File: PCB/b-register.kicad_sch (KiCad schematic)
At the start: 20 parts, among them U7 74LS245, U8 74LS173, U9 74LS173

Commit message: added more models to work with on my pcb
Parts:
- D022, D023, D024, D025, D026, D027, D028, D029: footprint LED_THT:LED_D1.8mm_W1.8mm_H2.4mm_Horizontal_O1.27mm_Z1.6mm -> LED_THT:LED_D3.0mm
- U7: footprint (none) -> Custom:DIP254P762X508-20
- U8, U9: footprint (none) -> Custom:SN74LS173AN
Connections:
- net GND: now also U7.10 (GND), U8.8 (GND), U9.8 (GND)
- net VCC: now also U7.20 (VCC), U8.16 (VCC), U9.16 (VCC)

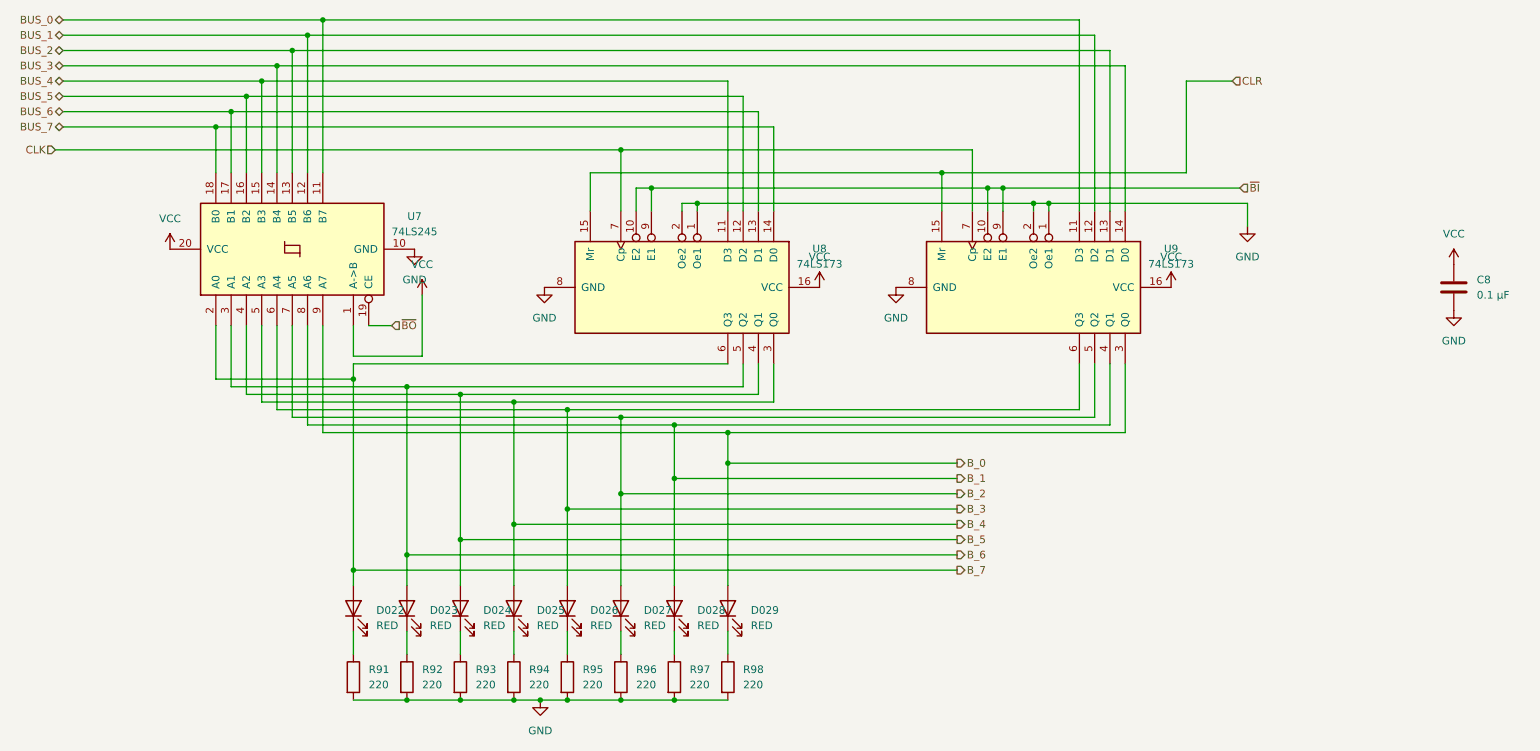
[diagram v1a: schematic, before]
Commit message: Fixed a bunch of ERC errors so know there is only one remaining.
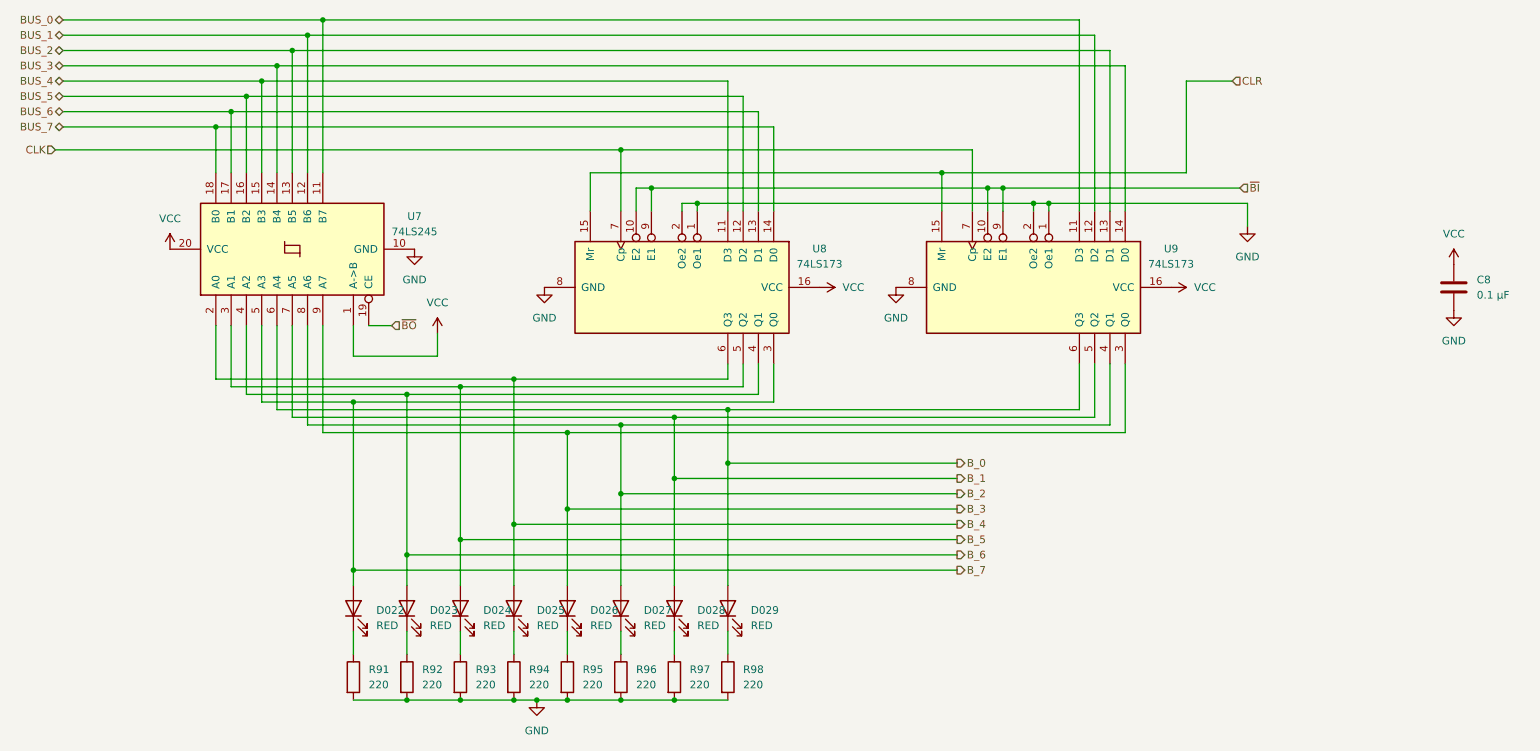
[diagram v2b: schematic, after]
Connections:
- net B_0: now also U7.6 (A4), U9.6 (Q3); no longer U7.9 (A7), U9.3 (Q0)
- net B_1: now also U7.7 (A5), U9.5 (Q2); no longer U7.8 (A6), U9.4 (Q1)
- net B_2: now also U7.8 (A6), U9.4 (Q1); no longer U7.7 (A5), U9.5 (Q2)
- net B_3: now also U7.9 (A7), U9.3 (Q0); no longer U7.6 (A4), U9.6 (Q3)
- net B_4: now also U7.2 (A0), U8.6 (Q3); no longer U7.5 (A3), U8.3 (Q0)
- net B_5: now also U7.3 (A1), U8.5 (Q2); no longer U7.4 (A2), U8.4 (Q1)
- net B_6: now also U7.4 (A2), U8.4 (Q1); no longer U7.3 (A1), U8.5 (Q2)
- net B_7: now also U7.5 (A3), U8.3 (Q0); no longer U7.2 (A0), U8.6 (Q3)

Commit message: Add decupling caps and reroute pcb. Updated BOM to match new number of caps
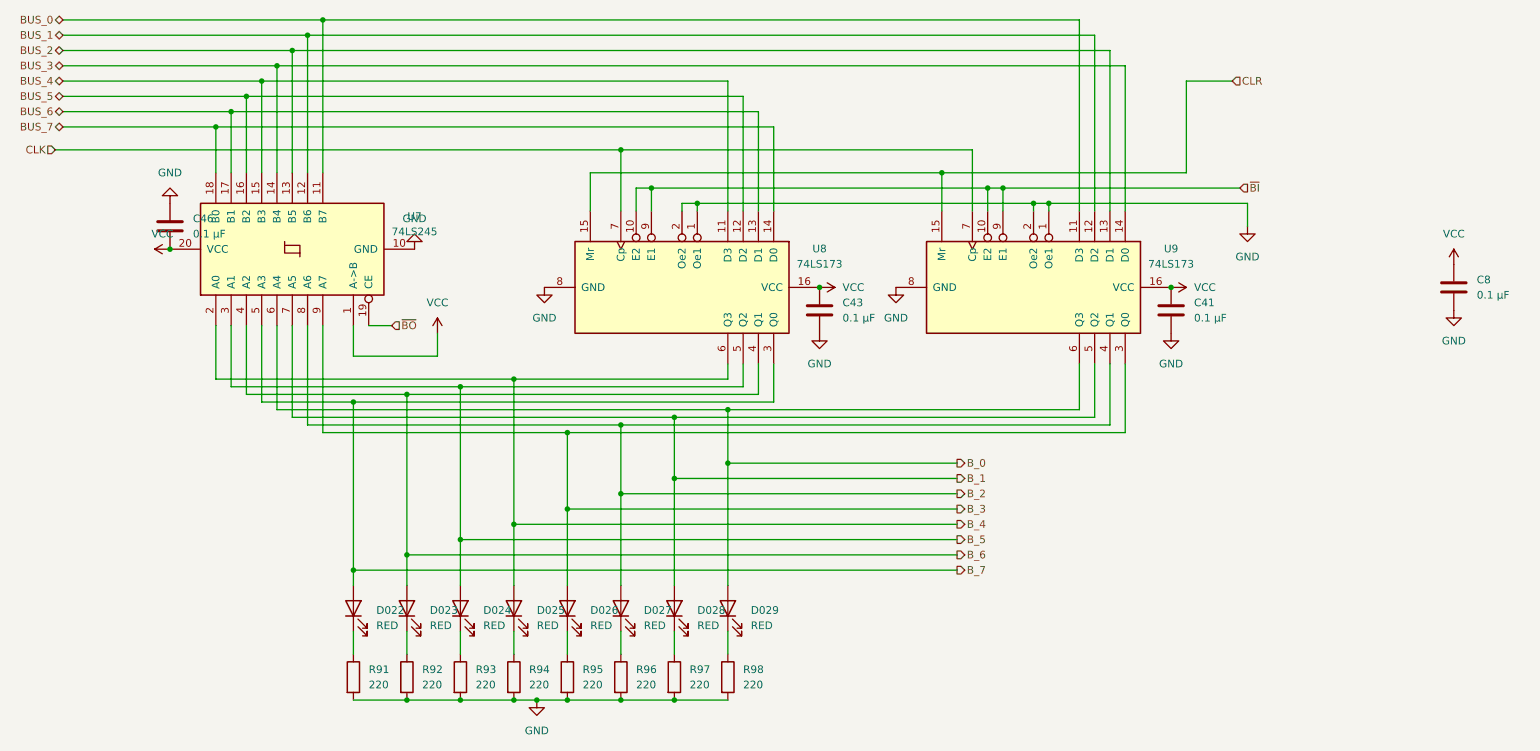
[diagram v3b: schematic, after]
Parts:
- added C41, C43, C46: 0.1 µF, Capacitor_THT:C_Radial_D5.0mm_H5.0mm_P2.00mm, symbol Device:C
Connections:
- net GND: now also C41.2, C43.2, C46.1
- net VCC: now also C41.1, C43.1, C46.2

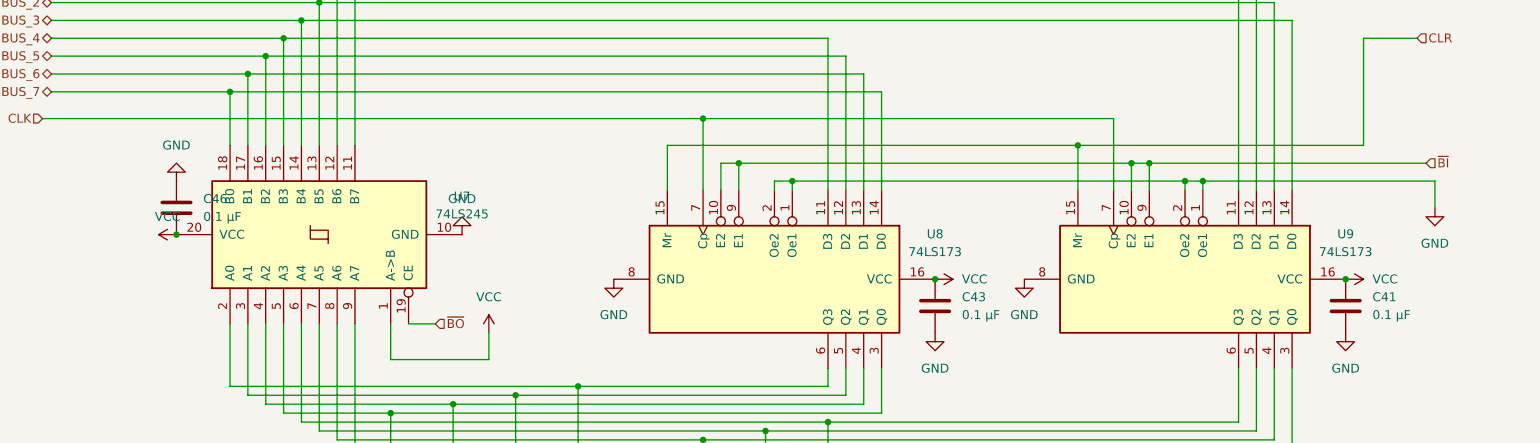
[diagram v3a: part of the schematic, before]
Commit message: Redoing PCB layout and fixed some signal flow convention errors
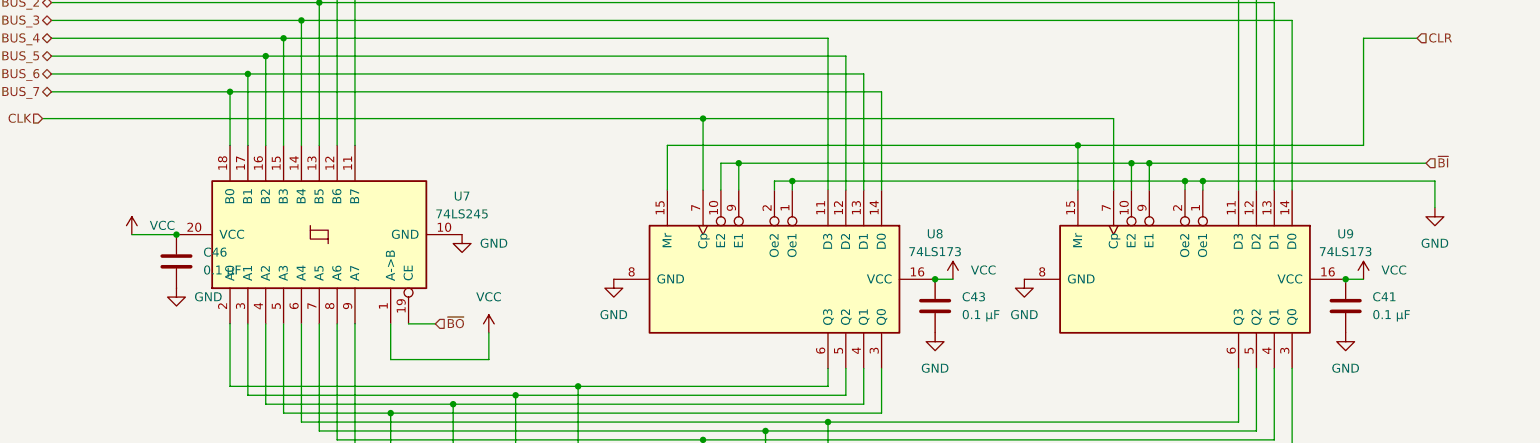
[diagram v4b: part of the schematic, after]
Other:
- moved on the sheet: C46
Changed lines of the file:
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@@
 	)
 	(junction
-		(at 46.99 58.42)
-		(diameter 0)
-		(color 0 0 0 0)
-	)
-	(junction
 		(at 185.42 48.26)
 		(diameter 0)
@@
 	)
 	(junction
+		(at 46.99 58.42)
+		(diameter 0)
+		(color 0 0 0 0)
+	)
+	(junction
 		(at 95.25 81.28)
 		(diameter 0)
@@
 	(wire
 		(pts
+			(xy 157.48 64.77) (xy 154.94 64.77)
+		)
+		(stroke
+			(width 0)
+			(type default)
+		)
+	)
+	(wire
+		(pts
 			(xy 69.85 87.63) (xy 121.92 87.63)
 		)
@@
 	(wire
 		(pts
+			(xy 40.64 58.42) (xy 46.99 58.42)
+		)
+		(stroke
+			(width 0)
+			(type default)
+		)
+	)
+	(wire
+		(pts
 			(xy 144.78 35.56) (xy 144.78 52.07)
 		)
@@
 	(wire
 		(pts
+			(xy 215.9 64.77) (xy 213.36 64.77)
+		)
+		(stroke
+			(width 0)
+			(type default)
+		)
+	)
+	(wire
+		(pts
 			(xy 29.21 22.86) (xy 69.85 22.86)
 		)
@@
 	(symbol
 		(lib_id "power:VCC")
-		(at 213.36 64.77 270)
+		(at 215.9 64.77 0)
 		(unit 1)
 		(exclude_from_sim no)
@@
 		(fields_autoplaced yes)
 		(property "Reference" "#PWR0134"
-			(at 209.55 64.77 0)
+			(at 215.9 68.58 0)
 			(effects
 				(font
@@
 		)
 		(property "Value" "VCC"
-			(at 217.17 64.7699 90)
+			(at 218.44 63.4999 0)
 			(effects
 				(font
@@
 		)
 		(property "Footprint" ""
-			(at 213.36 64.77 0)
+			(at 215.9 64.77 0)
 			(effects
 				(font
@@
 		)
 		(property "Datasheet" ""
-			(at 213.36 64.77 0)
+			(at 215.9 64.77 0)
 			(effects
 				(font
@@
 		)
 		(property "Description" "Power symbol creates a global label with name \"VCC\""
-			(at 213.36 64.77 0)
+			(at 215.9 64.77 0)
 			(effects
 				(font
@@
 	(symbol
 		(lib_id "power:GND")
-		(at 46.99 50.8 180)
+		(at 46.99 66.04 0)
 		(unit 1)
 		(exclude_from_sim no)
@@
 		(fields_autoplaced yes)
 		(property "Reference" "#PWR0177"
-			(at 46.99 44.45 0)
+			(at 46.99 72.39 0)
 			(effects
 				(font
@@
 		)
 		(property "Value" "GND"
-			(at 46.99 45.72 0)
+			(at 49.53 67.3099 0)
 			(effects
 				(font
 					(size 1.27 1.27)
 				)
+				(justify left)
 			)
 		)
 		(property "Footprint" ""
-			(at 46.99 50.8 0)
+			(at 46.99 66.04 0)
 			(effects
 				(font
@@
 		)
 		(property "Datasheet" ""
-			(at 46.99 50.8 0)
+			(at 46.99 66.04 0)
 			(effects
 				(font
@@
 		)
 		(property "Description" "Power symbol creates a global label with name \"GND\" , ground"
-			(at 46.99 50.8 0)
+			(at 46.99 66.04 0)
 			(effects
 				(font
@@
 	(symbol
 		(lib_id "power:GND")
-		(at 87.63 58.42 180)
+		(at 87.63 58.42 0)
 		(unit 1)
 		(exclude_from_sim no)
@@
 		(fields_autoplaced yes)
 		(property "Reference" "#PWR0137"
-			(at 87.63 52.07 0)
+			(at 87.63 64.77 0)
 			(effects
 				(font
@@
 		)
 		(property "Value" "GND"
-			(at 87.63 53.34 0)
+			(at 90.17 59.6899 0)
 			(effects
 				(font
 					(size 1.27 1.27)
 				)
+				(justify left)
 			)
 		)
@@
 	(symbol
 		(lib_id "power:VCC")
-		(at 46.99 58.42 90)
+		(at 40.64 58.42 0)
 		(unit 1)
 		(exclude_from_sim no)
@@
 		(fields_autoplaced yes)
 		(property "Reference" "#PWR0132"
-			(at 50.8 58.42 0)
+			(at 40.64 62.23 0)
 			(effects
 				(font
@@
 		)
 		(property "Value" "VCC"
-			(at 45.72 55.88 90)
+			(at 43.18 57.1499 0)
 			(effects
 				(font
 					(size 1.27 1.27)
 				)
+				(justify left)
 			)
 		)
 		(property "Footprint" ""
-			(at 46.99 58.42 0)
+			(at 40.64 58.42 0)
 			(effects
 				(font
@@
 		)
 		(property "Datasheet" ""
-			(at 46.99 58.42 0)
+			(at 40.64 58.42 0)
 			(effects
 				(font
@@
 		)
 		(property "Description" "Power symbol creates a global label with name \"VCC\""
-			(at 46.99 58.42 0)
+			(at 40.64 58.42 0)
 			(effects
 				(font
@@
 	(symbol
 		(lib_id "Device:C")
-		(at 46.99 54.61 0)
+		(at 46.99 62.23 180)
 		(unit 1)
 		(exclude_from_sim no)
@@
 		(fields_autoplaced yes)
 		(property "Reference" "C46"
-			(at 50.8 53.3399 0)
+			(at 50.8 60.9599 0)
 			(effects
 				(font
 					(size 1.27 1.27)
 				)
-				(justify left)
+				(justify right)
 			)
 		)
 		(property "Value" "0.1 µF"
-			(at 50.8 55.8799 0)
+			(at 50.8 63.4999 0)
 			(effects
 				(font
 					(size 1.27 1.27)
 				)
-				(justify left)
+				(justify right)
 			)
 		)
 		(property "Footprint" "Capacitor_THT:C_Radial_D5.0mm_H5.0mm_P2.00mm"
-			(at 47.9552 58.42 0)
+			(at 46.0248 58.42 0)
 			(effects
 				(font
@@
 		)
 		(property "Datasheet" "~"
-			(at 46.99 54.61 0)
+			(at 46.99 62.23 0)
 			(effects
 				(font
@@
 		)
 		(property "Description" "Unpolarized capacitor"
-			(at 46.99 54.61 0)
+			(at 46.99 62.23 0)
 			(effects
 				(font
@@
 	(symbol
 		(lib_id "power:VCC")
-		(at 154.94 64.77 270)
+		(at 157.48 64.77 0)
 		(unit 1)
 		(exclude_from_sim no)
@@
 		(fields_autoplaced yes)
 		(property "Reference" "#PWR0133"
-			(at 151.13 64.77 0)
+			(at 157.48 68.58 0)
 			(effects
 				(font
@@
 		)
 		(property "Value" "VCC"
-			(at 158.75 64.7699 90)
+			(at 160.02 63.4999 0)
 			(effects
 				(font
@@
 		)
 		(property "Footprint" ""
-			(at 154.94 64.77 0)
+			(at 157.48 64.77 0)
 			(effects
 				(font
@@
 		)
 		(property "Datasheet" ""
-			(at 154.94 64.77 0)
+			(at 157.48 64.77 0)
 			(effects
 				(font
@@
 		)
 		(property "Description" "Power symbol creates a global label with name \"VCC\""
-			(at 154.94 64.77 0)
+			(at 157.48 64.77 0)
 			(effects
 				(font
